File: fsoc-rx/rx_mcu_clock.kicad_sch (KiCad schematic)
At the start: 30 parts, among them J3 FTSH-105-01-L-DV-K, SW1 SW_RESET, SW2 USB_BOOT, U4 RP2354A, Y1 ABM8-272-T3, Y2 ASTX-H11-10.000MHz-T

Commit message: RX ROOT: HOST IO
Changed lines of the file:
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@@
+	)
+	(junction
+		(at 137.16 27.94)
+		(diameter 0)
+		(color 0 0 0 0)
 	)
 	(junction
@@
 	(wire
 		(pts
+			(xy 133.35 27.94) (xy 137.16 27.94)
+		)
+		(stroke
+			(width 0)
+			(type default)
+		)
+	)
+	(wire
+		(pts
 			(xy 140.97 148.59) (xy 152.4 148.59)
 		)
@@
 	(hierarchical_label "+3V3_ANA"
 		(shape input)
-		(at 137.16 27.94 180)
-		(effects
-			(font
+		(at 133.35 27.94 180)
+		(effects
+			(font

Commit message: RX ROOT: optical AFE
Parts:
- renumbered C18 to C11, C11 to C12, C12 to C13, C13 to C14, C14 to C15, C15 to C16, C16 to C17, C17 to C18, C9 to C7, C7 to C8, C8 to C9

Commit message: RX: footprint assignments
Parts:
- C10, C11, C12, C13, C14, C15, C16, C18, C19, C20, C22, C5, C6, C8: footprint (none) -> Capacitor_SMD:C_0603_1608Metric
- C17, C21, C7, C9: footprint (none) -> Capacitor_SMD:C_0805_2012Metric
- L1: footprint (none) -> fsoc_footprints:AOTA-B201610S3R3-101-T
- R3, R4, R5, R6, R7: footprint (none) -> Resistor_SMD:R_0603_1608Metric
- SW1, SW2: footprint (none) -> Button_Switch_SMD:SW_SPST_PTS645Sx43SMTR92
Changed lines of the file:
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@@
 			)
 		)
-		(property "Footprint" ""
+		(property "Footprint" "Capacitor_SMD:C_0603_1608Metric"
 			(at 162.8648 148.59 0)
 			(hide yes)
@@
 			)
 		)
-		(property "Footprint" ""
+		(property "Footprint" "Capacitor_SMD:C_0603_1608Metric"
 			(at 220.98 70.8152 0)
 			(hide yes)
@@
 			)
 		)
-		(property "Footprint" ""
+		(property "Footprint" "fsoc_footprints:AOTA-B201610S3R3-101-T"
 			(at 173.99 29.21 0)
 			(hide yes)
@@
 			)
 		)
-		(property "Footprint" ""
+		(property "Footprint" "Capacitor_SMD:C_0603_1608Metric"
 			(at 151.4348 148.59 0)
 			(hide yes)
@@
 			)
 		)
-		(property "Footprint" ""
+		(property "Footprint" "Capacitor_SMD:C_0603_1608Metric"
 			(at 175.5648 148.59 0)
 			(hide yes)
@@
 			)
 		)
-		(property "Footprint" ""
+		(property "Footprint" "Capacitor_SMD:C_0603_1608Metric"
 			(at 223.2152 109.22 0)
 			(hide yes)
@@
 			)
 		)
-		(property "Footprint" ""
+		(property "Footprint" "Capacitor_SMD:C_0603_1608Metric"
 			(at 113.9952 121.92 0)
 			(hide yes)
@@
 			)
 		)
-		(property "Footprint" ""
+		(property "Footprint" "Capacitor_SMD:C_0603_1608Metric"
 			(at 113.9952 104.14 0)
 			(hide yes)
@@
 			)
 		)
-		(property "Footprint" ""
+		(property "Footprint" "Capacitor_SMD:C_0805_2012Metric"
 			(at 228.6 58.7248 0)
 			(hide yes)
@@
 			)
 		)
-		(property "Footprint" ""
+		(property "Footprint" "Capacitor_SMD:C_0603_1608Metric"
 			(at 136.1948 27.94 0)
 			(hide yes)
@@
 			)
 		)
-		(property "Footprint" ""
+		(property "Footprint" "Capacitor_SMD:C_0603_1608Metric"
 			(at 117.1448 148.59 0)
 			(hide yes)
@@
 			)
 		)
-		(property "Footprint" ""
+		(property "Footprint" "Capacitor_SMD:C_0603_1608Metric"
 			(at 186.9948 148.59 0)
 			(hide yes)
@@
 			)
 		)
-		(property "Footprint" ""
+		(property "Footprint" "Capacitor_SMD:C_0805_2012Metric"
 			(at 122.8852 50.8 0)
 			(hide yes)
@@
 			)
 		)
-		(property "Footprint" ""
+		(property "Footprint" "Capacitor_SMD:C_0603_1608Metric"
 			(at 128.5748 148.59 0)
 			(hide yes)
@@
 			)
 		)
-		(property "Footprint" ""
+		(property "Footprint" "Button_Switch_SMD:SW_SPST_PTS645Sx43SMTR92"
 			(at 106.68 78.74 0)
 			(hide yes)
@@
 			)
 		)
-		(property "Footprint" ""
+		(property "Footprint" "Resistor_SMD:R_0603_1608Metric"
 			(at 116.84 44.958 90)
 			(hide yes)
@@
 			)
 		)
-		(property "Footprint" ""
+		(property "Footprint" "Capacitor_SMD:C_0603_1608Metric"
 			(at 198.4248 148.59 0)
 			(hide yes)
@@
 			)
 		)
-		(property "Footprint" ""
+		(property "Footprint" "Resistor_SMD:R_0603_1608Metric"
 			(at 120.65 85.598 90)
 			(hide yes)
@@
 			)
 		)
-		(property "Footprint" ""
+		(property "Footprint" "Resistor_SMD:R_0603_1608Metric"
 			(at 128.27 112.522 90)
 			(hide yes)
@@
 			)
 		)
-		(property "Footprint" ""
+		(property "Footprint" "Capacitor_SMD:C_0603_1608Metric"
 			(at 140.0048 148.59 0)
 			(hide yes)
@@
 			)
 		)
-		(property "Footprint" ""
+		(property "Footprint" "Capacitor_SMD:C_0805_2012Metric"
 			(at 115.2652 25.4 0)
 			(hide yes)
@@
 			)
 		)
-		(property "Footprint" ""
+		(property "Footprint" "Capacitor_SMD:C_0603_1608Metric"
 			(at 228.6 48.5648 0)
 			(hide yes)
@@
 			)
 		)
-		(property "Footprint" ""
+		(property "Footprint" "Resistor_SMD:R_0603_1608Metric"
 			(at 124.46 70.612 90)
 			(hide yes)
@@
 			)
 		)
-		(property "Footprint" ""
+		(property "Footprint" "Resistor_SMD:R_0603_1608Metric"
 			(at 124.46 75.692 90)
 			(hide yes)
@@
 			)
 		)
-		(property "Footprint" ""
+		(property "Footprint" "Capacitor_SMD:C_0805_2012Metric"
 			(at 191.4652 39.37 0)
 			(hide yes)
@@
 			)
 		)
-		(property "Footprint" ""
+		(property "Footprint" "Button_Switch_SMD:SW_SPST_PTS645Sx43SMTR92"
 			(at 104.14 60.96 0)
 			(hide yes)

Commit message: RX PCB
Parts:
- U4: footprint Package_DFN_QFN:QFN-60-1EP_7x7mm_P0.4mm_EP3.4x3.4mm -> Package_DFN_QFN:QFN-60-1EP_7x7mm_P0.4mm_EP3.4x3.4mm_ThermalVias
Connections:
- net USB_DM renamed USB_DN
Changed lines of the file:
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@@
 		)
 	)
-	(hierarchical_label "USB_DM"
+	(hierarchical_label "USB_DN"
 		(shape bidirectional)
 		(at 118.11 72.39 180)
@@
 			)
 		)
-		(property "Footprint" "Package_DFN_QFN:QFN-60-1EP_7x7mm_P0.4mm_EP3.4x3.4mm"
+		(property "Footprint" "Package_DFN_QFN:QFN-60-1EP_7x7mm_P0.4mm_EP3.4x3.4mm_ThermalVias"
 			(at 160.02 88.9 0)
 			(hide yes)

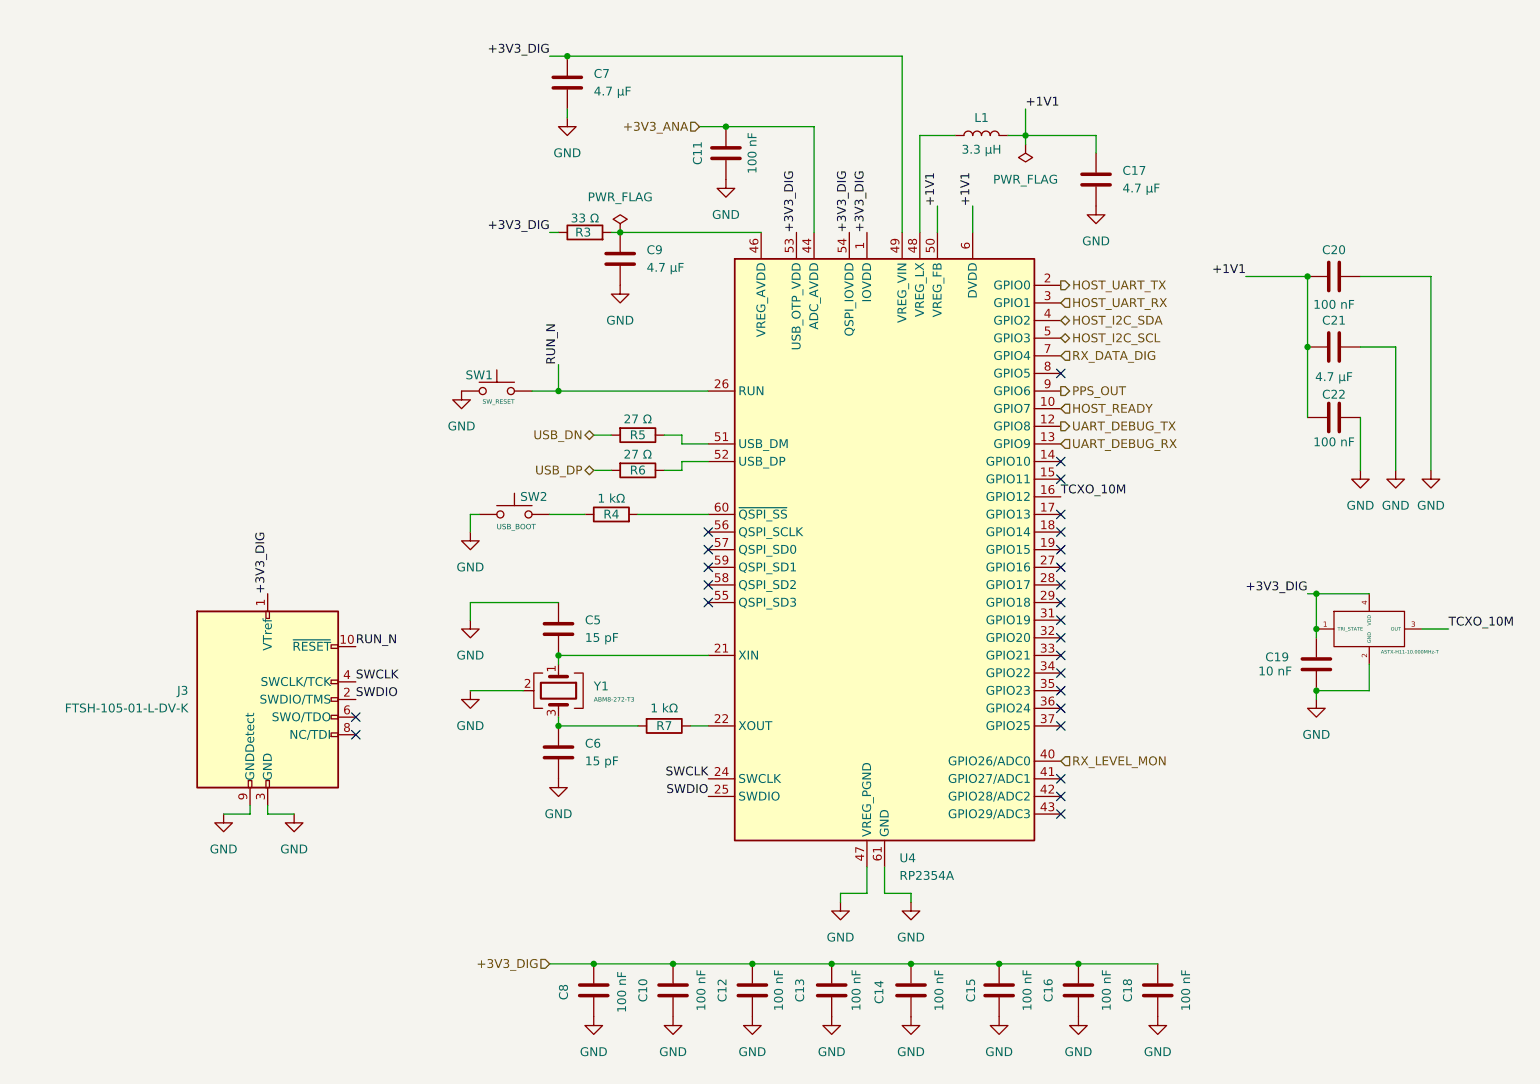
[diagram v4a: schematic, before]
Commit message: RX PCB: SiT5346
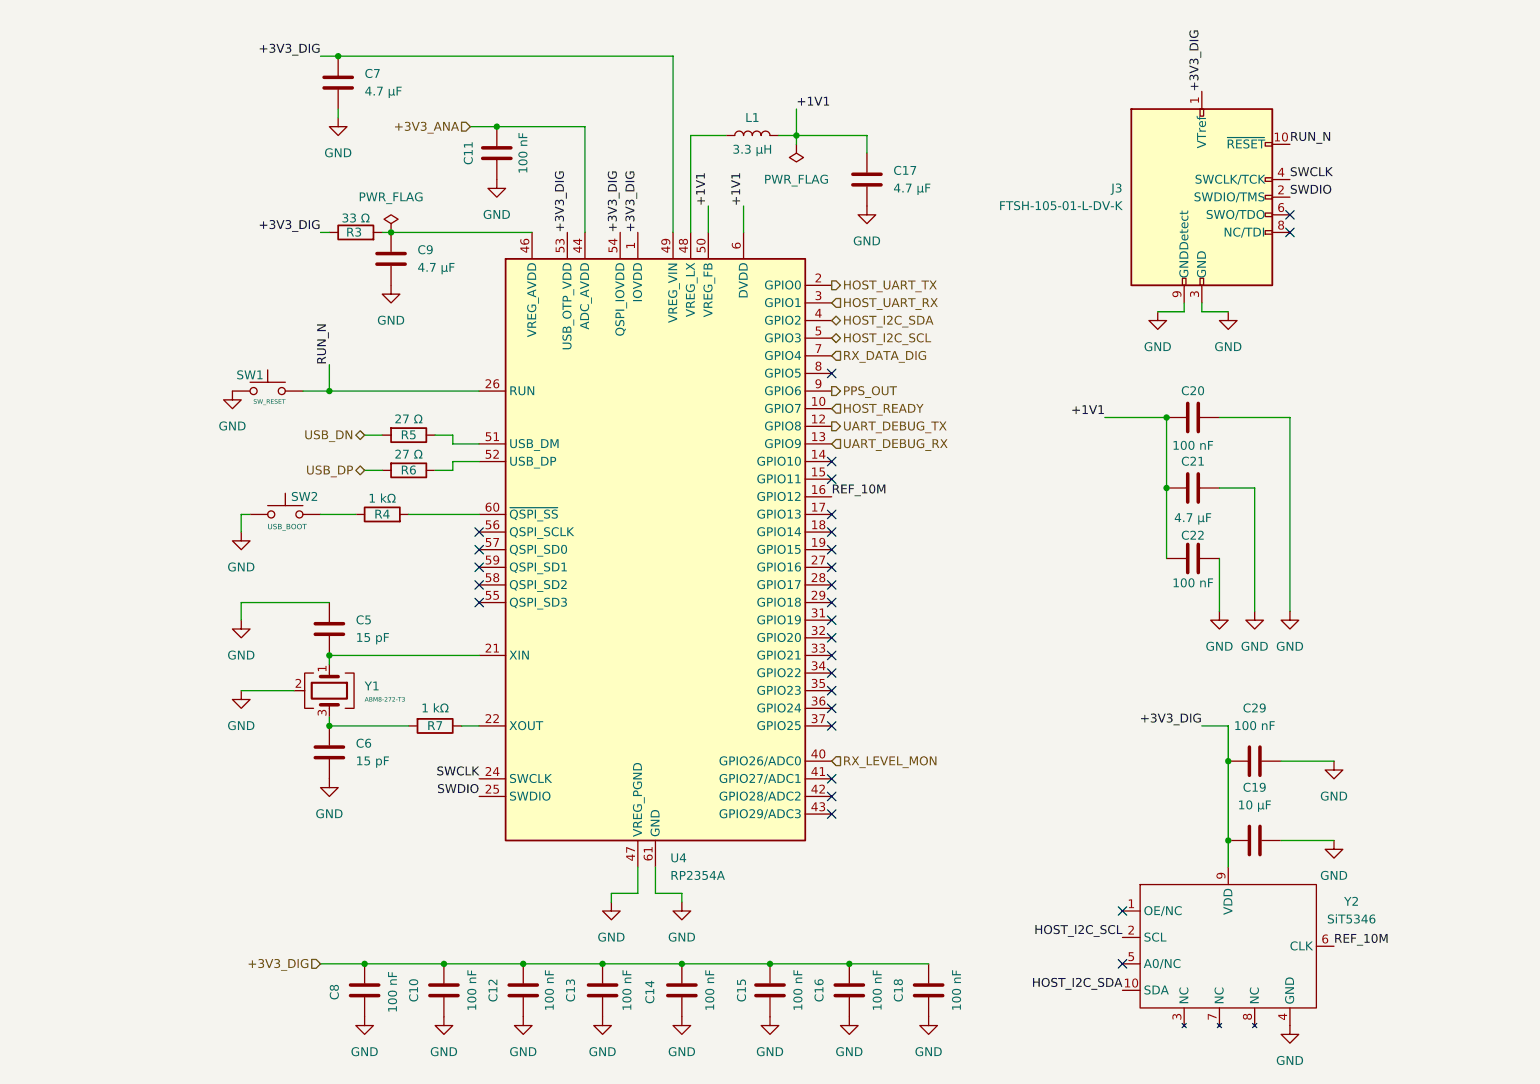
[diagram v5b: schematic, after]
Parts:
- removed Y2: ASTX-H11-10.000MHz-T, fsoc_footprints:ASTX-H11_3225, symbol fsoc_symbols:ASTX-H11
- added C29: 100 nF, Capacitor_SMD:C_0603_1608Metric, symbol Device:C
- added Y2: SiT5346, fsoc_footprints:SiT5346_5.0x3.2mm_10L, symbol fsoc_symbols:SiT5346_DCTCXO
- C19: value 10 nF -> 10 µF; footprint Capacitor_SMD:C_0603_1608Metric -> Capacitor_SMD:C_0805_2012Metric
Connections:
- net +3V3_DIG: now also C29.1, Y2.9 (VDD)
- net GND: now also C29.2, Y2.4 (GND)
- net HOST_I2C_SCL: now also Y2.2 (SCL)
- net HOST_I2C_SDA: now also Y2.10 (SDA)
- net TCXO_10M renamed REF_10M
- net REF_10M: now also Y2.6 (CLK)
- no-connect marks 26 -> 28
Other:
- moved on the sheet: C10, C11, C12, C13, C14, C15, C16, C17, C18, C20, C21, C22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

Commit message: manufacturer part number for Sit5346
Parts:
- Y2: MPN (none) -> TBD - SiT5346 10MHz 3.3V LVCMOS DCTCXO; Manufacturer Part Number TBD - SiT5346 10MHz DCTCXO configuration -> (none)
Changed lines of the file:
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@@
 			)
 		)
-		(property "Manufacturer Part Number" "TBD - SiT5346 10MHz DCTCXO configuration"
+		(property "JLCPCB Part" "TBD - Global Sourcing if not stocked"
 			(at 209.55 146.05 0)
 			(hide yes)
@@
 			)
 		)
-		(property "JLCPCB Part" "TBD - Global Sourcing if not stocked"
+		(property "MPN" "TBD - SiT5346 10MHz 3.3V LVCMOS DCTCXO"
 			(at 209.55 146.05 0)
 			(hide yes)
